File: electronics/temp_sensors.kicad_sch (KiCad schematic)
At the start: 4 parts, among them J17 Conn_01x03, J18 Conn_01x03, J19 Conn_01x03

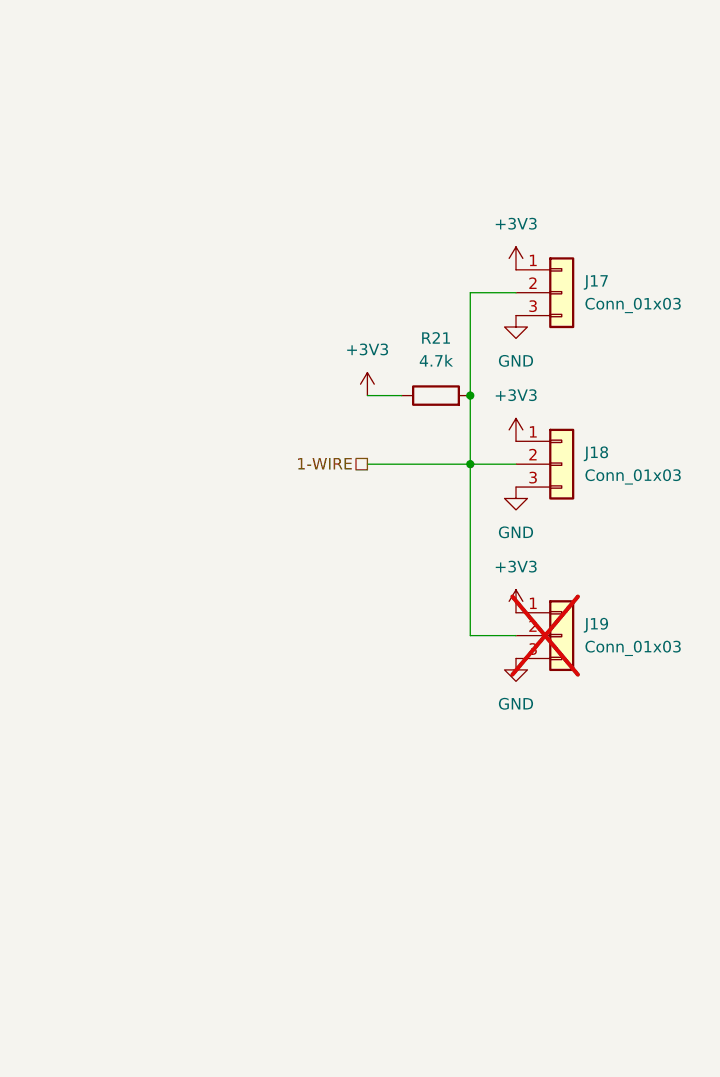
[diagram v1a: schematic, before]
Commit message: start to create BOM and finalising symbol fields
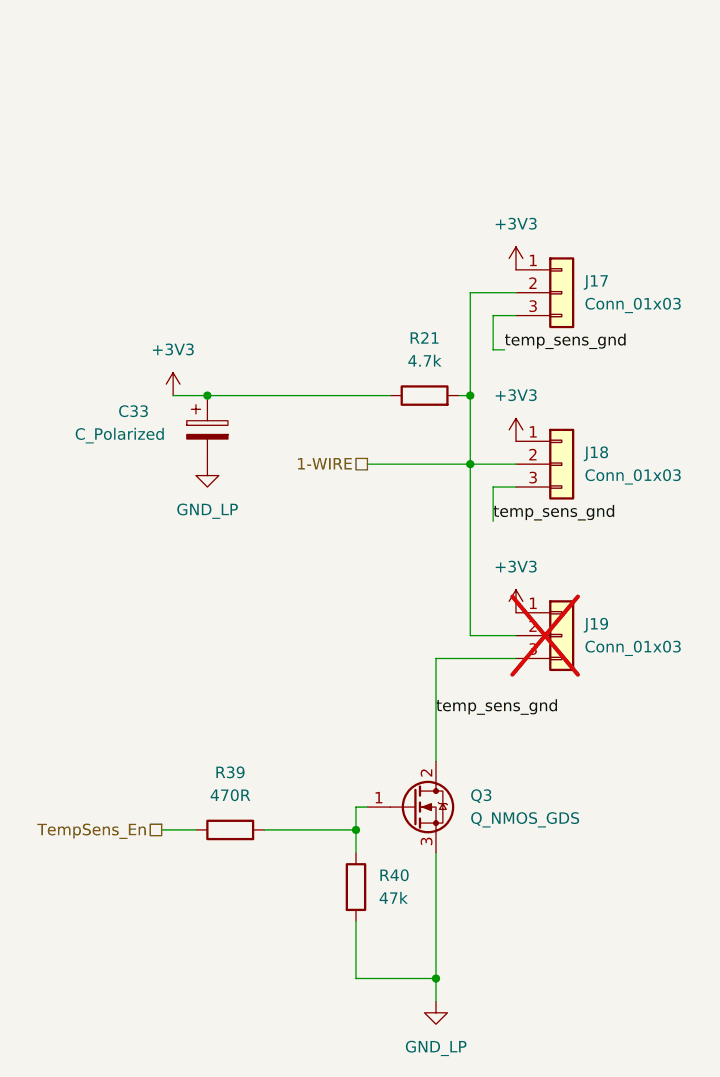
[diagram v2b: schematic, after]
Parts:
- added C33: C_Polarized, Capacitor_THT:CP_Radial_D5.0mm_P2.50mm, symbol Device:C_Polarized
- added Q3: Q_NMOS_GDS, Package_TO_SOT_SMD:TO-252-2, symbol Device:Q_NMOS_GDS
- added R39: 470R, Resistor_SMD:R_0805_2012Metric, symbol Device:R
- added R40: 47k, Resistor_SMD:R_0805_2012Metric, symbol Device:R
- R21: footprint Resistor_SMD:R_0805_2012Metric_Pad1.20x1.40mm_HandSolder -> Resistor_SMD:R_0805_2012Metric
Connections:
- net at R21.1: now also C33.1
- net GND renamed temp_sens_gnd
- net temp_sens_gnd: now also Q3.2 (D)
- new net: Q3.1 (G), R39.2, R40.1
- new net GND_LP: C33.2, Q3.3 (S), R40.2
- new net TempSens_En: R39.1
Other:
- moved on the sheet: R21

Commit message: progres on layouting
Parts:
- Q3: footprint Package_TO_SOT_SMD:TO-252-2 -> Package_TO_SOT_SMD:SOT-23
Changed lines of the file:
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@@
 	(label "temp_sens_gnd"
 		(at 69.85 74.93 0)
-		(fields_autoplaced yes)
 		(effects
 			(font
@@
 	(label "temp_sens_gnd"
 		(at 63.5 96.52 0)
-		(fields_autoplaced yes)
 		(effects
 			(font
@@
 	(label "temp_sens_gnd"
 		(at 71.12 55.88 0)
-		(fields_autoplaced yes)
 		(effects
 			(font
@@
 		(shape passive)
 		(at 33.02 109.22 180)
-		(fields_autoplaced yes)
 		(effects
 			(font
@@
 		(shape passive)
 		(at 55.88 68.58 180)
-		(fields_autoplaced yes)
 		(effects
 			(font
@@
 			)
 		)
-		(property "Footprint" "Package_TO_SOT_SMD:TO-252-2"
+		(property "Footprint" "Package_TO_SOT_SMD:SOT-23"
 			(at 66.04 104.14 0)
 			(effects
@@
 		(exclude_from_sim no)
 		(in_bom yes)
-		(on_board yes)
+		(on_board no)
 		(dnp yes)
 		(fields_autoplaced yes)

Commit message: layouting progress. some 3d models upload
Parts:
- removed C33: C_Polarized, Capacitor_THT:CP_Radial_D5.0mm_P2.50mm, symbol Device:C_Polarized
- added C13: C_Polarized, Capacitor_THT:CP_Radial_D5.0mm_P2.50mm, symbol Device:C_Polarized
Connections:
- net +3V3: now also C13.1
- net GND_LP: now also C13.2
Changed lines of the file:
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@@
 	(paper "A4")
 	(junction
-		(at 38.1 60.96)
+		(at 71.12 34.29)
 		(diameter 0)
 		(color 0 0 0 0)
@@
 	(wire
 		(pts
-			(xy 38.1 60.96) (xy 58.42 60.96)
+			(xy 34.29 60.96) (xy 58.42 60.96)
 		)
 		(stroke
@@
 	(wire
 		(pts
+			(xy 71.12 46.99) (xy 71.12 34.29)
+		)
+		(stroke
+			(width 0)
+			(type default)
+		)
+	)
+	(wire
+		(pts
 			(xy 63.5 111.76) (xy 63.5 125.73)
 		)
@@
 	(wire
 		(pts
+			(xy 71.12 25.4) (xy 71.12 34.29)
+		)
+		(stroke
+			(width 0)
+			(type default)
+		)
+	)
+	(wire
+		(pts
 			(xy 72.39 90.17) (xy 63.5 90.17)
 		)
@@
 	(wire
 		(pts
+			(xy 63.5 34.29) (xy 71.12 34.29)
+		)
+		(stroke
+			(width 0)
+			(type default)
+		)
+	)
+	(wire
+		(pts
 			(xy 63.5 125.73) (xy 63.5 128.27)
 		)
@@
 	(wire
 		(pts
-			(xy 34.29 60.96) (xy 38.1 60.96)
-		)
-		(stroke
-			(width 0)
-			(type default)
-		)
-	)
-	(wire
-		(pts
 			(xy 54.61 109.22) (xy 54.61 111.76)
 		)
@@
 		(pts
 			(xy 69.85 71.12) (xy 69.85 74.93)
+		)
+		(stroke
+			(width 0)
+			(type default)
+		)
+	)
+	(wire
+		(pts
+			(xy 72.39 46.99) (xy 71.12 46.99)
 		)
 		(stroke
@@
 	(label "temp_sens_gnd"
 		(at 69.85 74.93 0)
+		(fields_autoplaced yes)
 		(effects
 			(font
@@
 	(label "temp_sens_gnd"
 		(at 63.5 96.52 0)
+		(fields_autoplaced yes)
 		(effects
 			(font
@@
 	(label "temp_sens_gnd"
 		(at 71.12 55.88 0)
+		(fields_autoplaced yes)
 		(effects
 			(font
@@
 		(shape passive)
 		(at 33.02 109.22 180)
+		(fields_autoplaced yes)
 		(effects
 			(font
@@
 		(shape passive)
 		(at 55.88 68.58 180)
+		(fields_autoplaced yes)
 		(effects
 			(font
@@
 			)
 			(justify right)
-		)
-	)
-	(symbol
-		(lib_id "Device:C_Polarized")
-		(at 38.1 64.77 0)
-		(unit 1)
-		(exclude_from_sim no)
-		(in_bom yes)
-		(on_board yes)
-		(dnp no)
-		(property "Reference" "C33"
-			(at 28.194 62.738 0)
-			(effects
-				(font
-					(size 1.27 1.27)
-				)
-				(justify left)
-			)
-		)
-		(property "Value" "C_Polarized"
-			(at 23.368 65.278 0)
-			(effects
-				(font
-					(size 1.27 1.27)
-				)
-				(justify left)
-			)
-		)
-		(property "Footprint" "Capacitor_THT:CP_Radial_D5.0mm_P2.50mm"
-			(at 39.0652 68.58 0)
-			(effects
-				(font
-					(size 1.27 1.27)
-				)
-				(hide yes)
-			)
-		)
-		(property "Datasheet" "~"
-			(at 38.1 64.77 0)
-			(effects
-				(font
-					(size 1.27 1.27)
-				)
-				(hide yes)
-			)
-		)
-		(property "Description" "Polarized capacitor"
-			(at 38.1 64.77 0)
-			(effects
-				(font
-					(size 1.27 1.27)
-				)
-				(hide yes)
-			)
-		)
-		(pin "2"
-		)
-		(pin "1"
-		)
-		(instances
-			(project "electronics"
-				(path "/eeb1234c-eae0-4ac6-a30d-2a978d66d889/04c402f1-b99a-4823-99a0-0c7312782f29/10cf4ae7-01f2-4d37-acf1-79de902611a8"
-					(reference "C33")
-					(unit 1)
-				)
-			)
 		)
 	)
@@
 	)
 	(symbol
-		(lib_id "power:GND2")
-		(at 38.1 68.58 0)
+		(lib_id "power:+3V3")
+		(at 71.12 25.4 0)
 		(unit 1)
 		(exclude_from_sim no)
@@
 		(dnp no)
 		(fields_autoplaced yes)
-		(property "Reference" "#PWR077"
-			(at 38.1 74.93 0)
-			(effects
-				(font
-					(size 1.27 1.27)
-				)
-				(hide yes)
-			)
-		)
-		(property "Value" "GND_LP"
-			(at 38.1 73.66 0)
+		(property "Reference" "#PWR038"
+			(at 71.12 29.21 0)
+			(effects
+				(font
+					(size 1.27 1.27)
+				)
+				(hide yes)
+			)
+		)
+		(property "Value" "+3V3"
+			(at 71.12 20.32 0)
 			(effects
 				(font
@@
 		)
 		(property "Footprint" ""
-			(at 38.1 68.58 0)
+			(at 71.12 25.4 0)
 			(effects
 				(font
@@
 		)
 		(property "Datasheet" ""
-			(at 38.1 68.58 0)
-			(effects
-				(font
-					(size 1.27 1.27)
-				)
-				(hide yes)
-			)
-		)
-		(property "Description" "Power symbol creates a global label with name \"GND2\" , ground"
-			(at 38.1 68.58 0)
+			(at 71.12 25.4 0)
+			(effects
+				(font
+					(size 1.27 1.27)
+				)
+				(hide yes)
+			)
+		)
+		(property "Description" "Power symbol creates a global label with name \"+3V3\""
+			(at 71.12 25.4 0)
 			(effects
 				(font
@@
 			(project "electronics"
 				(path "/eeb1234c-eae0-4ac6-a30d-2a978d66d889/04c402f1-b99a-4823-99a0-0c7312782f29/10cf4ae7-01f2-4d37-acf1-79de902611a8"
-					(reference "#PWR077")
+					(reference "#PWR038")
 					(unit 1)
 				)
@@
 	)
 	(symbol
-		(lib_id "power:+3V3")
-		(at 72.39 46.99 0)
+		(lib_id "Device:C_Polarized")
+		(at 63.5 38.1 0)
 		(unit 1)
 		(exclude_from_sim no)
@@
 		(on_board yes)
 		(dnp no)
-		(fields_autoplaced yes)
-		(property "Reference" "#PWR038"
-			(at 72.39 50.8 0)
-			(effects
-				(font
-					(size 1.27 1.27)
-				)
-				(hide yes)
-			)
-		)
-		(property "Value" "+3V3"
-			(at 72.39 41.91 0)
-			(effects
-				(font
-					(size 1.27 1.27)
-				)
-			)
-		)
-		(property "Footprint" ""
-			(at 72.39 46.99 0)
-			(effects
-				(font
-					(size 1.27 1.27)
-				)
-				(hide yes)
-			)
-		)
-		(property "Datasheet" ""
-			(at 72.39 46.99 0)
-			(effects
-				(font
-					(size 1.27 1.27)
-				)
-				(hide yes)
-			)
-		)
-		(property "Description" "Power symbol creates a global label with name \"+3V3\""
-			(at 72.39 46.99 0)
-			(effects
-				(font
-					(size 1.27 1.27)
-				)
-				(hide yes)
-			)
+		(property "Reference" "C13"
+			(at 53.594 36.068 0)
+			(effects
+				(font
+					(size 1.27 1.27)
+				)
+				(justify left)
+			)
+		)
+		(property "Value" "C_Polarized"
+			(at 48.768 38.608 0)
+			(effects
+				(font
+					(size 1.27 1.27)
+				)
+				(justify left)
+			)
+		)
+		(property "Footprint" "Capacitor_THT:CP_Radial_D5.0mm_P2.50mm"
+			(at 64.4652 41.91 0)
+			(effects
+				(font
+					(size 1.27 1.27)
+				)
+				(hide yes)
+			)
+		)
+		(property "Datasheet" "~"
+			(at 63.5 38.1 0)
+			(effects
+				(font
+					(size 1.27 1.27)
+				)
+				(hide yes)
+			)
+		)
+		(property "Description" "Polarized capacitor"
+			(at 63.5 38.1 0)
+			(effects
+				(font
+					(size 1.27 1.27)
+				)
+				(hide yes)
+			)
+		)
+		(pin "2"
 		)
 		(pin "1"
@@
 			(project "electronics"
 				(path "/eeb1234c-eae0-4ac6-a30d-2a978d66d889/04c402f1-b99a-4823-99a0-0c7312782f29/10cf4ae7-01f2-4d37-acf1-79de902611a8"
-					(reference "#PWR038")
+					(reference "C13")
 					(unit 1)
 				)
@@
 					(unit 1)
 				)
+			)
+		)
+	)
+	(symbol
+		(lib_id "power:GND2")
+		(at 63.5 41.91 0)
+		(unit 1)
+		(exclude_from_sim no)
+		(in_bom yes)
+		(on_board yes)
+		(dnp no)
+		(fields_autoplaced yes)
+		(property "Reference" "#PWR077"
+			(at 63.5 48.26 0)
+			(effects
+				(font
+					(size 1.27 1.27)
+				)
+				(hide yes)
+			)
+		)
+		(property "Value" "GND_LP"
+			(at 63.5 46.99 0)
+			(effects
+				(font
+					(size 1.27 1.27)
+				)
+			)
+		)
+		(property "Footprint" ""
+			(at 63.5 41.91 0)
+			(effects
+				(font
+					(size 1.27 1.27)
+				)
+				(hide yes)
+			)
+		)
+		(property "Datasheet" ""
+			(at 63.5 41.91 0)
+			(effects
+				(font
+					(size 1.27 1.27)
+				)
+				(hide yes)
+			)
+		)
+		(property "Description" "Power symbol creates a global label with name \"GND2\" , ground"
+			(at 63.5 41.91 0)
+			(effects
+				(font
+					(size 1.27 1.27)
+				)
+				(hide yes)
+			)
+		)
+		(pin "1"
+		)
+		(instances
+			(project "electronics"
+				(path "/eeb1234c-eae0-4ac6-a30d-2a978d66d889/04c402f1-b99a-4823-99a0-0c7312782f29/10cf4ae7-01f2-4d37-acf1-79de902611a8"
+					(reference "#PWR077")
+					(unit 1)
+				)
